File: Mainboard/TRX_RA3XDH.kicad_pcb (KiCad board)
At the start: 2 copper layers, 100 x 100 mm, 203 parts, among them J1 RF_INOUT, J10 MIC_GAIN, J12 PWR, J13 S-Met., J2 VFO, J3 PWR, J4 MIC, J5 VOL, J6 SPK, J8 PTT, J9 CW_KEY, K2 G5V-2, Q1 2N4416, Q10 2N3904, Q12 2N3904, Q2 2N918, Q3 2N4416, Q4 2N918, Q5 2N3904, Q6 2N3904, Q7 2N3904, Q8 2N3904, Q9 2N3906, U1 NE5534, U2 LM386, U3 NE5534, Y1 8.867Mhz, Y2 8.867Mhz, Y3 8.867Mhz, Y4 8.867Mhz, Y5 8.867Mhz, Y6 8.867Mhz, Y7 8.867Mhz, Y8 8.867Mhz

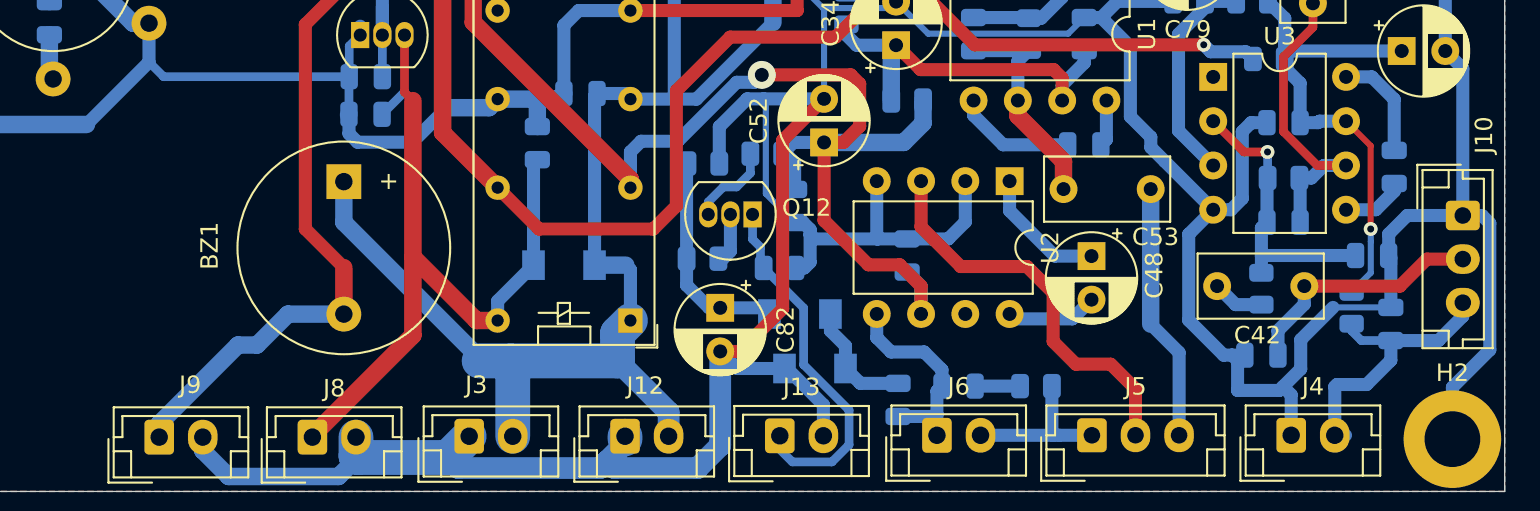
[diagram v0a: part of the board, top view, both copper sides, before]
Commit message: Added connectors labels
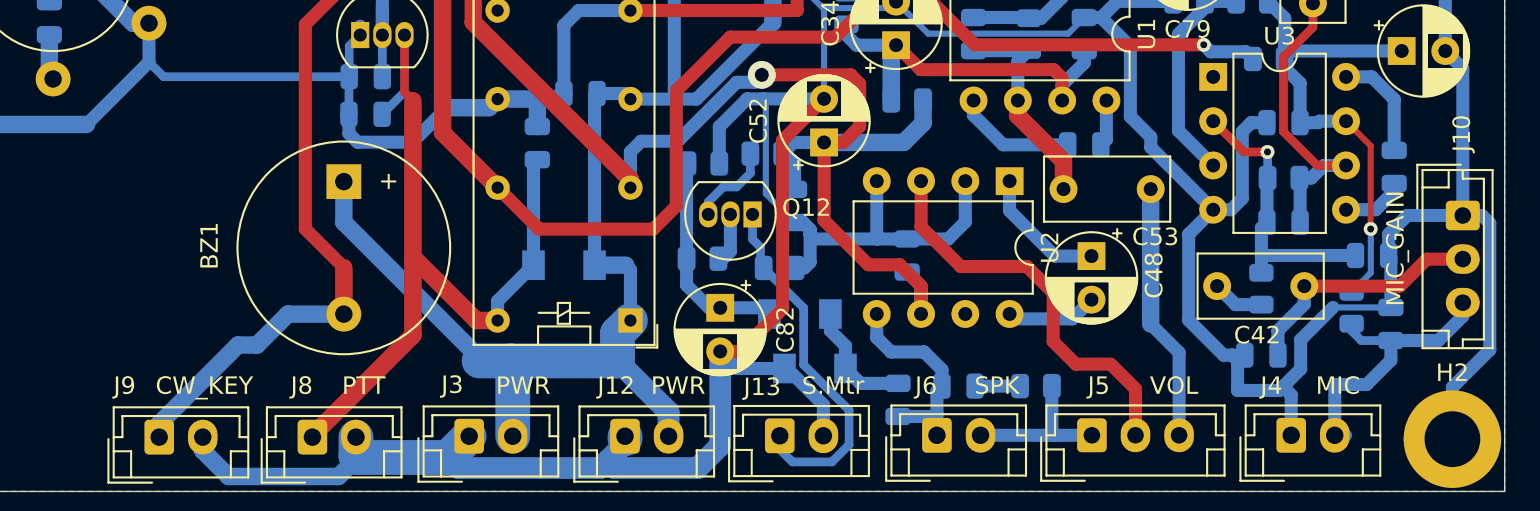
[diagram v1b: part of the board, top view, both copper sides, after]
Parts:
- H5: value MountingHole_Pad -> gnd
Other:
- board text added: "CW_KEY"
- board text added: "MIC"
- board text added: "MIC_GAIN"
- board text added: "PTT"
- board text added: "PWR"
- board text added: "S.Mtr"
- board text added: "SPK"
- board text added: "VOL"
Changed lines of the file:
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@@
   (general
     (thickness 1.6)
-    (drawings 6)
+    (drawings 15)
     (tracks 1121)
     (zones 0)
@@
     (add_net "Net-(Q7-Pad3)")
     (add_net "Net-(Q9-Pad2)")
+    (add_net "Net-(U1-Pad1)")
+    (add_net "Net-(U2-Pad7)")
+    (add_net "Net-(U3-Pad1)")
   )
   (module Package_TO_SOT_THT:TO-72-4 (layer F.Cu)
@@
       (effects (font (size 1 1) (thickness 0.15)))
     )
-    (fp_text value MountingHole_Pad (at 0 2.05) (layer F.Fab)
+    (fp_text value gnd (at 0 2.05) (layer F.Fab)
       (effects (font (size 1 1) (thickness 0.15)))
     )
@@
     (descr "JST EH series connector, B2B-EH-A (http://www.jst-mfg.com/product/pdf/eng/eEH.pdf), generated with kicad-footprint-generator")
     (tags "connector JST EH vertical")
-    (fp_text reference J13 (at 1.25 -2.8) (layer F.SilkS)
+    (fp_text reference J13 (at -1.0052 -2.8) (layer F.SilkS)
       (effects (font (size 1 1) (thickness 0.15)))
     )
@@
     (descr "JST EH series connector, B2B-EH-A (http://www.jst-mfg.com/product/pdf/eng/eEH.pdf), generated with kicad-footprint-generator")
     (tags "connector JST EH vertical")
-    (fp_text reference J12 (at 1.1557 -2.8956) (layer F.SilkS)
+    (fp_text reference J12 (at -0.508 -2.8956) (layer F.SilkS)
       (effects (font (size 1 1) (thickness 0.15)))
     )
@@
     (descr "JST EH series connector, B2B-EH-A (http://www.jst-mfg.com/product/pdf/eng/eEH.pdf), generated with kicad-footprint-generator")
     (tags "connector JST EH vertical")
-    (fp_text reference J8 (at 1.25 -2.8) (layer F.SilkS)
+    (fp_text reference J8 (at -0.6096 -2.9464) (layer F.SilkS)
       (effects (font (size 1 1) (thickness 0.15)))
     )
@@
     (descr "JST EH series connector, B3B-EH-A (http://www.jst-mfg.com/product/pdf/eng/eEH.pdf), generated with kicad-footprint-generator")
     (tags "connector JST EH vertical")
-    (fp_text reference J10 (at -4.6101 -1.2192 90) (layer F.SilkS)
+    (fp_text reference J10 (at -4.7117 0.0508 90) (layer F.SilkS)
       (effects (font (size 1 1) (thickness 0.15)))
     )
@@
     (descr "JST EH series connector, B2B-EH-A (http://www.jst-mfg.com/product/pdf/eng/eEH.pdf), generated with kicad-footprint-generator")
     (tags "connector JST EH vertical")
-    (fp_text reference J9 (at 1.778 -2.9972) (layer F.SilkS)
+    (fp_text reference J9 (at -1.9812 -2.9464) (layer F.SilkS)
       (effects (font (size 1 1) (thickness 0.15)))
     )
@@
     (descr "JST EH series connector, B2B-EH-A (http://www.jst-mfg.com/product/pdf/eng/eEH.pdf), generated with kicad-footprint-generator")
     (tags "connector JST EH vertical")
-    (fp_text reference J6 (at 1.25 -2.8) (layer F.SilkS)
+    (fp_text reference J6 (at -0.6202 -2.8406) (layer F.SilkS)
       (effects (font (size 1 1) (thickness 0.15)))
     )
@@
     (descr "JST EH series connector, B3B-EH-A (http://www.jst-mfg.com/product/pdf/eng/eEH.pdf), generated with kicad-footprint-generator")
     (tags "connector JST EH vertical")
-    (fp_text reference J5 (at 2.5 -2.8) (layer F.SilkS)
+    (fp_text reference J5 (at 0.3958 -2.8406) (layer F.SilkS)
       (effects (font (size 1 1) (thickness 0.15)))
     )
@@
     (descr "JST EH series connector, B2B-EH-A (http://www.jst-mfg.com/product/pdf/eng/eEH.pdf), generated with kicad-footprint-generator")
     (tags "connector JST EH vertical")
-    (fp_text reference J4 (at 1.25 -2.8) (layer F.SilkS)
+    (fp_text reference J4 (at -1.1282 -2.8406) (layer F.SilkS)
       (effects (font (size 1 1) (thickness 0.15)))
     )
@@
     (descr "JST EH series connector, B2B-EH-A (http://www.jst-mfg.com/product/pdf/eng/eEH.pdf), generated with kicad-footprint-generator")
     (tags "connector JST EH vertical")
-    (fp_text reference J3 (at 0.4064 -2.9464) (layer F.SilkS)
+    (fp_text reference J3 (at -0.9652 -2.9464) (layer F.SilkS)
       (effects (font (size 1 1) (thickness 0.15)))
     )
@@
     )
   )
+  (gr_text MIC_GAIN (at 173.736 131.064 90) (layer F.SilkS)
+    (effects (font (size 1 1) (thickness 0.15)))
+  )
+  (gr_text MIC (at 170.434 138.938) (layer F.SilkS)
+    (effects (font (size 1 1) (thickness 0.15)))
+  )
+  (gr_text VOL (at 161.036 138.938) (layer F.SilkS)
+    (effects (font (size 1 1) (thickness 0.15)))
+  )
+  (gr_text SPK (at 150.876 138.938) (layer F.SilkS)
+    (effects (font (size 1 1) (thickness 0.15)))
+  )
+  (gr_text S.Mtr (at 141.478 138.938) (layer F.SilkS)
+    (effects (font (size 1 1) (thickness 0.15)))
+  )
+  (gr_text PWR (at 132.588 138.938) (layer F.SilkS)
+    (effects (font (size 1 1) (thickness 0.15)))
+  )
+  (gr_text PWR (at 123.698 138.938) (layer F.SilkS)
+    (effects (font (size 1 1) (thickness 0.15)))
+  )
+  (gr_text PTT (at 114.554 138.938) (layer F.SilkS)
+    (effects (font (size 1 1) (thickness 0.15)))
+  )
+  (gr_text CW_KEY (at 105.41 138.938) (layer F.SilkS)
+    (effects (font (size 1 1) (thickness 0.15)))
+  )
   (dimension 100 (width 0.15) (layer Dwgs.User)
